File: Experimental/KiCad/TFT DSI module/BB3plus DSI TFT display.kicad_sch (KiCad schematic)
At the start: 54 parts, among them IC1 AZ1117CH2-3.3TRG1, IC2 TCA9554APWR, IC3 TPS61169DCKR, SW1 B3FS-4052P, SW2 B3FS-4052P, SW3 B3FS-4052P, SW4 B3FS-4052P, X1 5051102091, X2 505110-4091, X3 F3311A7H121010E200

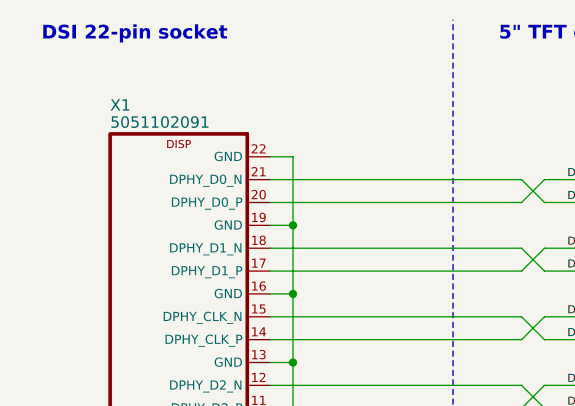
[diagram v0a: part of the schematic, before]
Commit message: Enclosure front and rear panel update, projects location reorganized
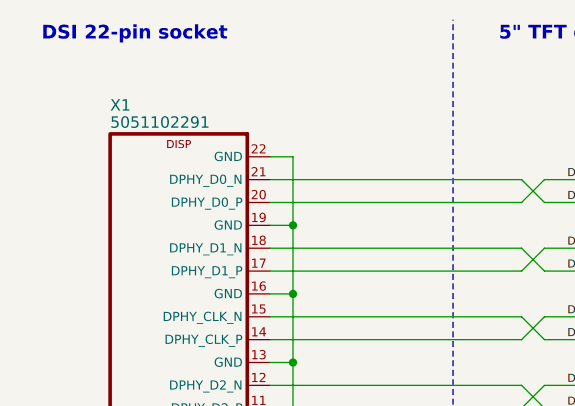
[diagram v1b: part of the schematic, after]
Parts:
- X1: value 5051102091 -> 5051102291
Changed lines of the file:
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@@
 	(title_block
 		(title "${project_name}")
-		(date "2025-11-27")
+		(date "2025-12-07")
 		(rev "${project_version}")
 		(company "${project_creator}")
@@
 			)
 		)
-		(property "Value" "5051102091"
+		(property "Value" "5051102291"
 			(at 25.4 26.67 0)
 			(effects
